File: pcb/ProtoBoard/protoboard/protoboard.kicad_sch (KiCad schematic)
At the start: 0 parts

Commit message: added components
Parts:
- added M1: Stepper_Motor_bipolar, symbol Motor:Stepper_Motor_bipolar
- added U1: AMS-OSRAM_Breakout_AS5047P, symbol Custom_Library:AMS-OSRAM_Breakout_AS5047P
- added U2, U3: Pololu_Breakout_DRV8874, symbol Custom_Library:Pololu_Breakout_DRV8874
- added U4: NUCLEO-F446RE, NUCLEO-F446RE:MODULE_NUCLEO-F446RE, symbol Custom_Library:NUCLEO-F446RE
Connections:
- new net CN10_GND: U4.CN10_20 (CN10_GND), U4.CN10_9 (CN10_GND)
- new net CN6_GND: U4.CN6_6 (CN6_GND), U4.CN6_7 (CN6_GND)
- new net CN7_GND: U4.CN7_19 (CN7_GND), U4.CN7_20 (CN7_GND), U4.CN7_22 (CN7_GND), U4.CN7_8 (CN7_GND)
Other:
- company: (none) -> Polar Robotics
- title: (none) -> PSD17 Protoboard

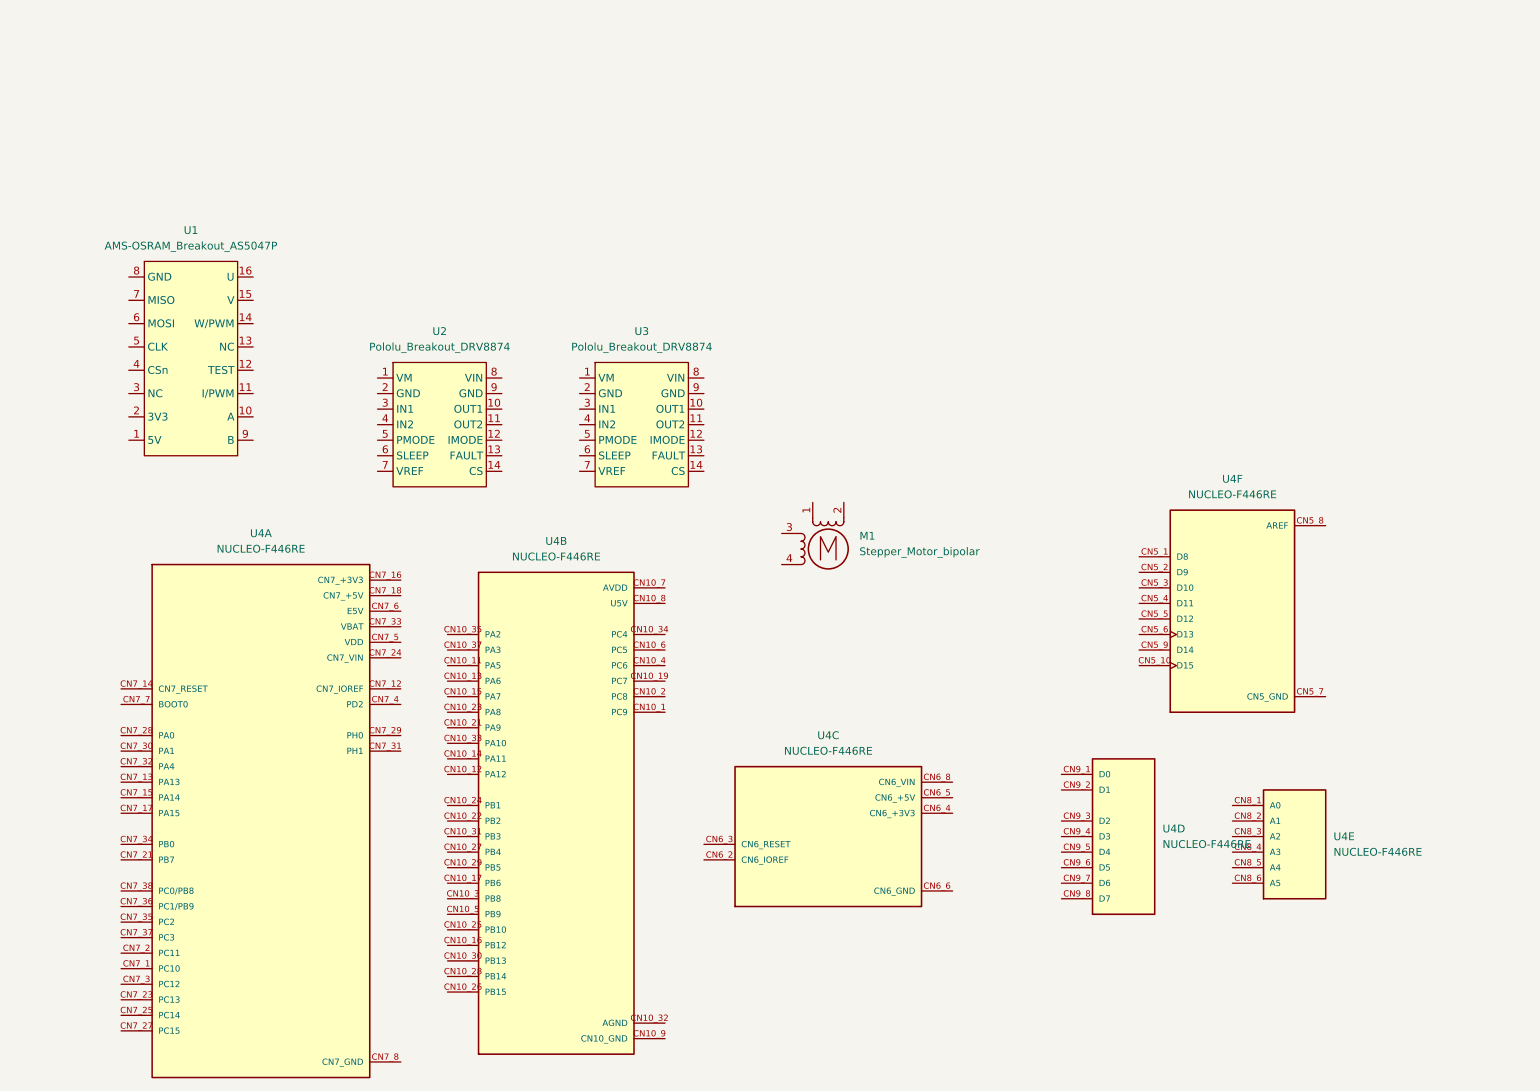
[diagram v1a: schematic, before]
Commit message: added more schematics
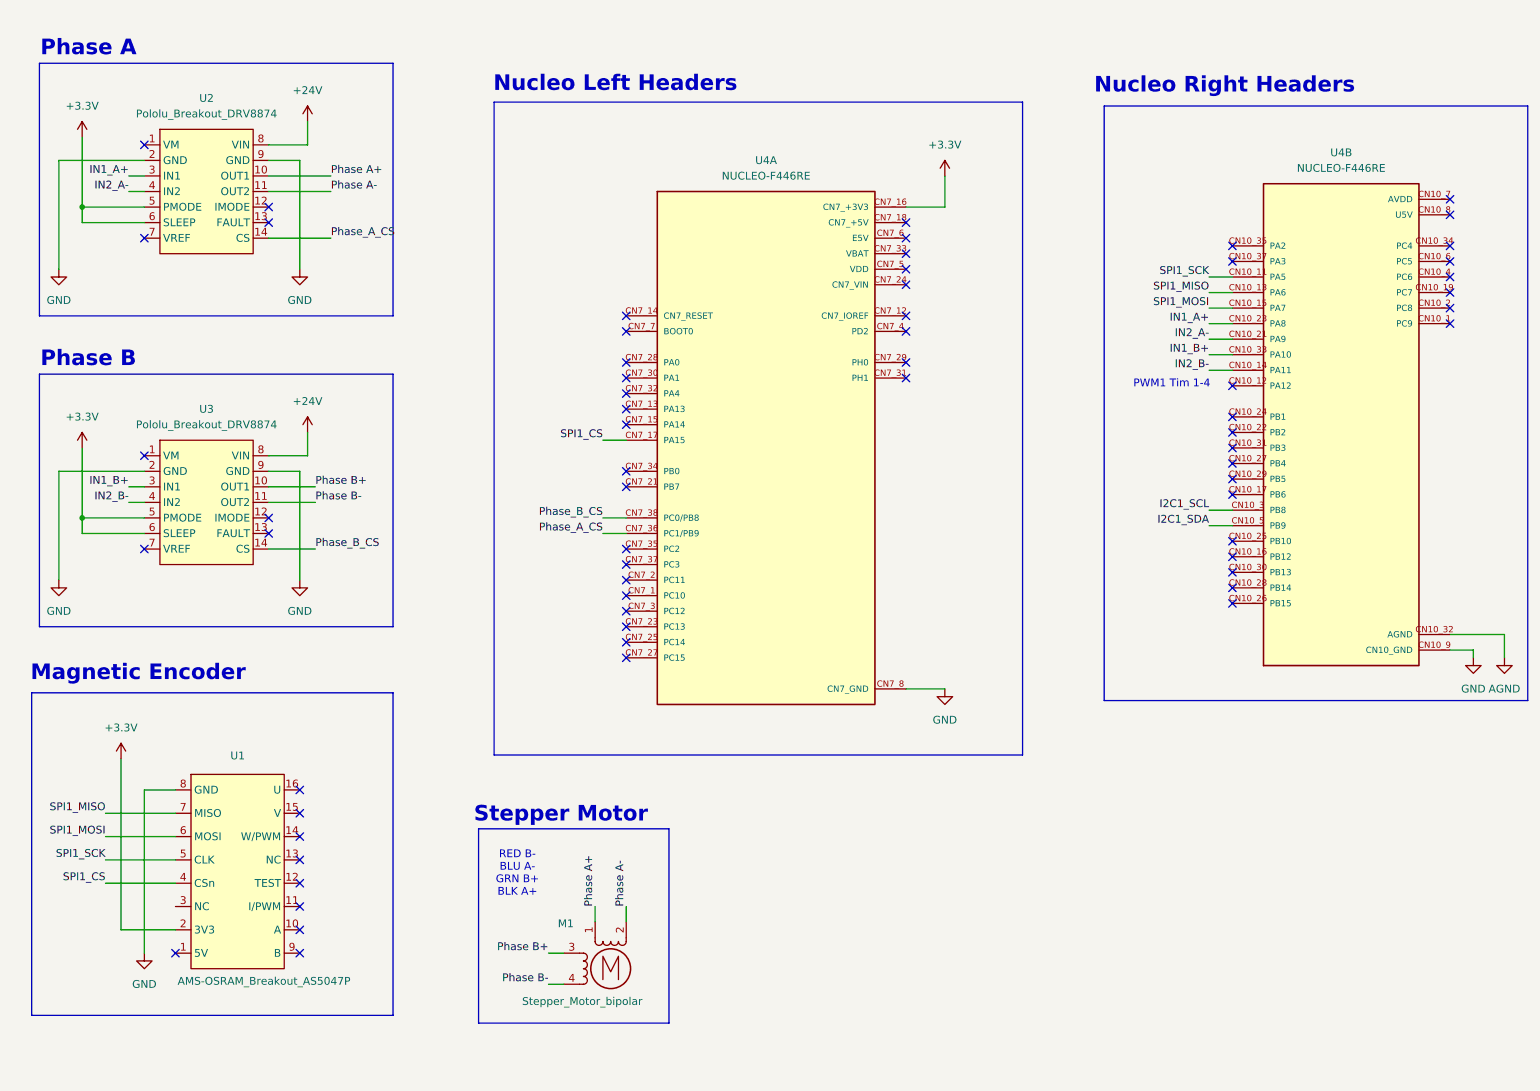
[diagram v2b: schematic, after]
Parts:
- removed unit 6 of U4
- removed unit 5 of U4
- removed unit 3 of U4
- removed unit 4 of U4
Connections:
- net CN7_GND is gone; now on net CN10_GND: U4.CN7_19 (CN7_GND), U4.CN7_20 (CN7_GND), U4.CN7_22 (CN7_GND), U4.CN7_8 (CN7_GND)
- net CN10_GND: now also U1.8 (GND), U2.2 (GND), U2.9 (GND), U3.2 (GND), U3.9 (GND)
- net Phase B+: now reaches U3.10 (OUT1)
- net Phase B+: now also M1.3
- net Phase B-: now reaches U3.11 (OUT2)
- net Phase B-: now also M1.4
- net Phase_B_CS: now reaches U3.14 (CS)
- net Phase_B_CS: now also U4.CN7_38 (PC0/PB8)
- net IN1_B+: now reaches U3.3 (IN1)
- net IN1_B+: now also U4.CN10_33 (PA10)
- net IN2_B-: now reaches U3.4 (IN2)
- net IN2_B-: now also U4.CN10_14 (PA11)
- net +3.3V: now reaches U3.5 (PMODE)
- net +3.3V: now also U1.2 (3V3), U2.5 (PMODE), U2.6 (SLEEP), U3.6 (SLEEP), U4.CN7_16 (CN7_+3V3)
- net +24V: now reaches U3.8 (VIN)
- net +24V: now also U2.8 (VIN)
- net SPI1_SCK: now reaches U4.CN10_11 (PA5)
- net SPI1_SCK: now also U1.5 (CLK)
- net SPI1_MISO: now reaches U4.CN10_13 (PA6)
- net SPI1_MISO: now also U1.7 (MISO)
- net SPI1_MOSI: now reaches U4.CN10_15 (PA7)
- net SPI1_MOSI: now also U1.6 (MOSI)
- net IN2_A-: now reaches U4.CN10_21 (PA9)
- net IN2_A-: now also U2.4 (IN2)
- net IN1_A+: now reaches U4.CN10_23 (PA8)
- net IN1_A+: now also U2.3 (IN1)
- net I2C1_SCL: now reaches U4.CN10_3 (PB8)
- net AGND: now reaches U4.CN10_32 (AGND)
- net I2C1_SDA: now reaches U4.CN10_5 (PB9)
- net Phase A+: now reaches M1.1
- net Phase A+: now also U2.10 (OUT1)
- net Phase A-: now reaches M1.2 (-)
- net Phase A-: now also U2.11 (OUT2)
- net SPI1_CS: now reaches U1.4 (CSn)
- net SPI1_CS: now also U4.CN7_17 (PA15)
- net Phase_A_CS: now reaches U2.14 (CS)
- net Phase_A_CS: now also U4.CN7_36 (PC1/PB9)
- no-connect marks 0 -> 65
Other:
- note added: "Magnetic Encoder"
- note added: "Nucleo Left Headers"
- note added: "Nucleo Right Headers"
- note added: "PWM1 Tim 1-4"
- note added: "Phase A"
- note added: "Phase B"
- note added: "RED B- BLU A- GRN B+ BLK A+"
- note added: "Stepper Motor"
- moved on the sheet: M1, U1, U2, U4A, U4B

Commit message: added perfboard
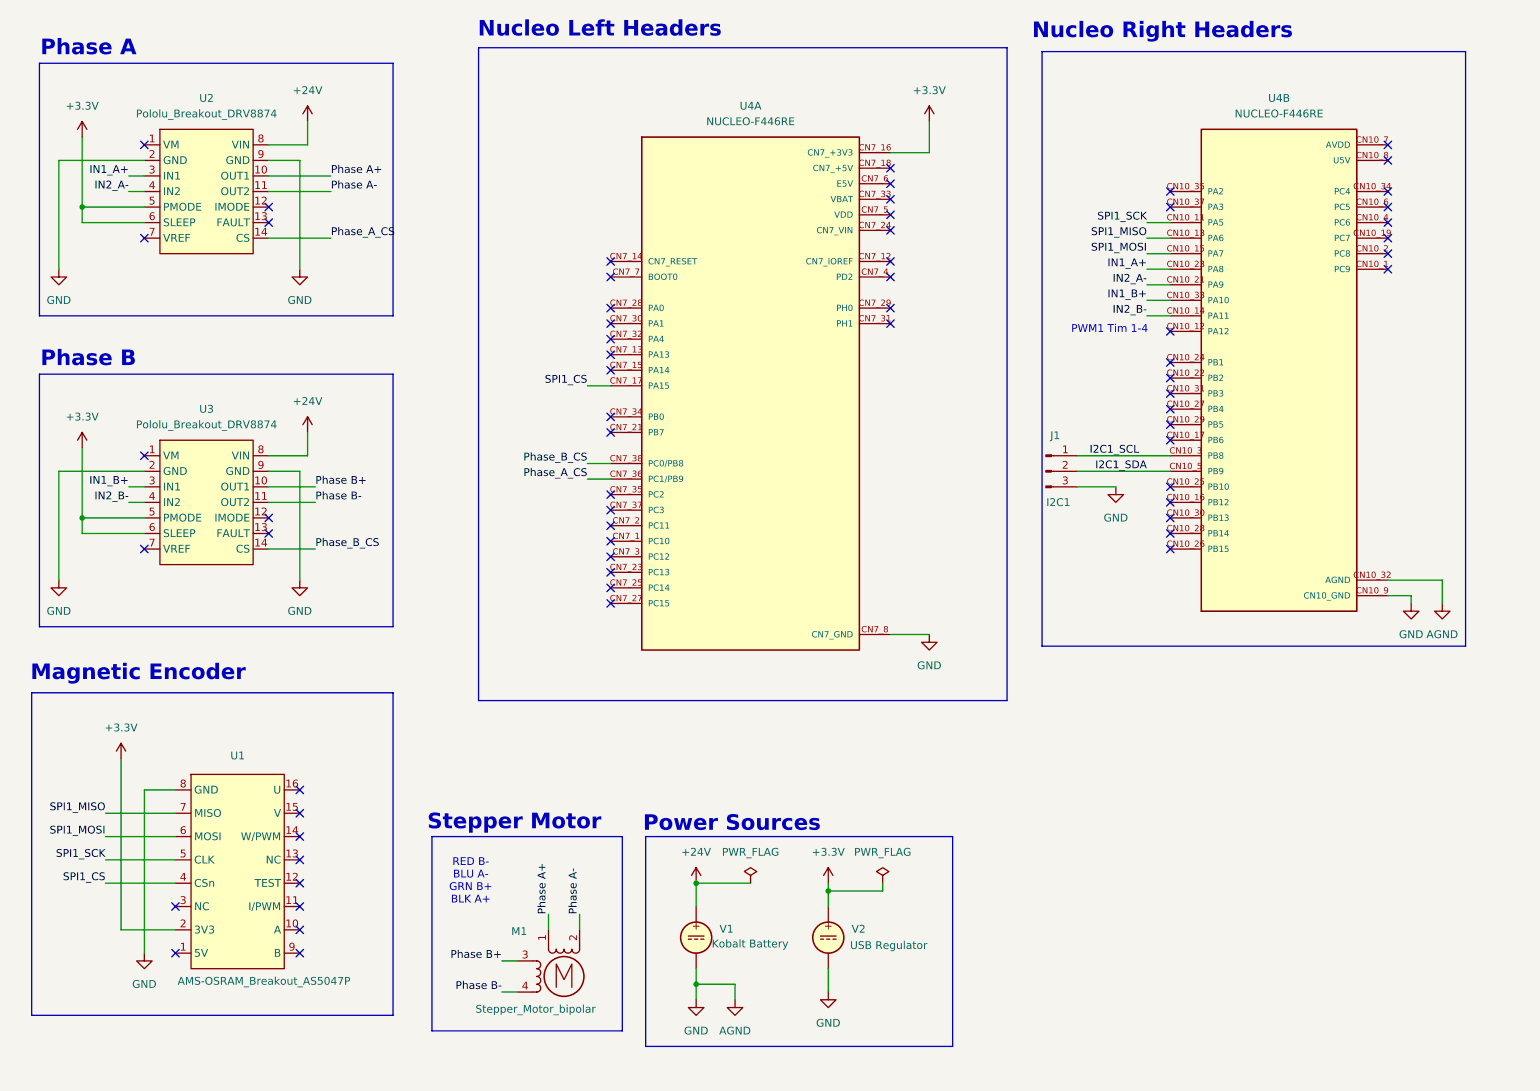
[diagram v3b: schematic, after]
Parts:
- added J1: I2C1, Connector_PinHeader_2.54mm:PinHeader_1x03_P2.54mm_Vertical, symbol Connector:Conn_01x03_Pin
- added V1: Kobalt Battery, symbol Simulation_SPICE:VDC
- added V2: USB Regulator, symbol Simulation_SPICE:VDC
- U2, U3: footprint (none) -> Custom_Library:Pololu_Breakout_DRV8874
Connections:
- net CN10_GND is gone; now on net AGND: U1.8 (GND), U2.2 (GND), U2.9 (GND), U3.2 (GND), U3.9 (GND), U4.CN10_20 (CN10_GND), U4.CN10_9 (CN10_GND), U4.CN7_19 (CN7_GND), U4.CN7_20 (CN7_GND), U4.CN7_22 (CN7_GND), U4.CN7_8 (CN7_GND)
- net +24V: now also V1.1
- net +3.3V: now also V2.1
- net AGND: now also J1.3 (Pin_3), V1.2, V2.2
- net I2C1_SCL: now also J1.1 (Pin_1)
- net I2C1_SDA: now also J1.2 (Pin_2)
- no-connect marks 65 -> 66
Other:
- note added: "Power Sources"
- moved on the sheet: M1, U4A, U4B

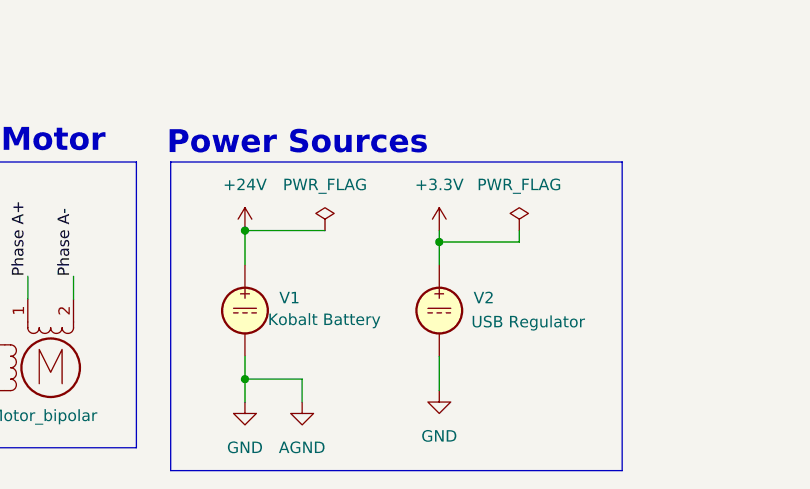
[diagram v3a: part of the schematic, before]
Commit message: started perfboard layout
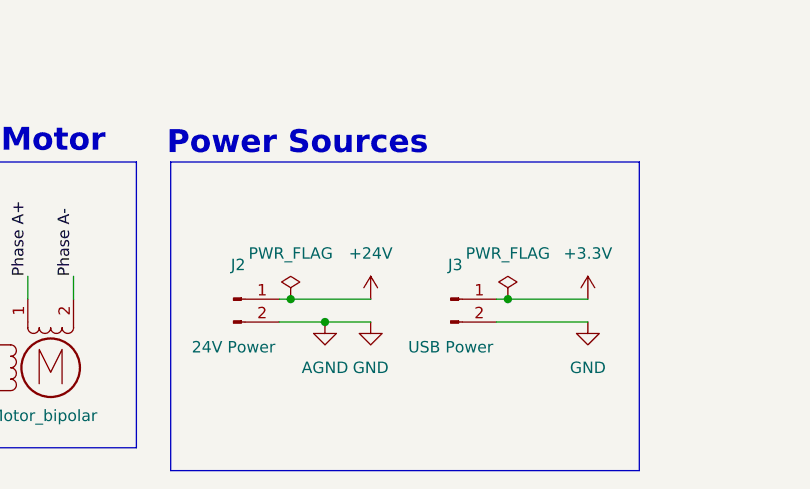
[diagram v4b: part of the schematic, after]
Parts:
- removed V1: Kobalt Battery, symbol Simulation_SPICE:VDC
- removed V2: USB Regulator, symbol Simulation_SPICE:VDC
- added J2: 24V Power, Connector_PinHeader_2.54mm:PinHeader_1x02_P2.54mm_Vertical, symbol Connector:Conn_01x02_Pin
- added J3: USB Power, Connector_PinHeader_2.54mm:PinHeader_1x02_P2.54mm_Vertical, symbol Connector:Conn_01x02_Pin
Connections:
- net +24V: now also J2.1 (Pin_1)
- net +3.3V: now also J3.1 (Pin_1)
- net AGND: now also J2.2 (Pin_2), J3.2 (Pin_2)
